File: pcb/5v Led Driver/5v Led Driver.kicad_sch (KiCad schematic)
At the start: 43 parts, among them J1 USB_C_Receptacle_USB2.0_16P, J2 Conn_01x02_Pin, J3 Conn_01x02_Pin, J4 Conn_01x03_Pin, J5 Conn_01x02_Pin, SW2 PTS815 SJM 250 SMTR LFS, U1 RP2040, U2 W25Q16JVUXIQ TR, U3 RT6150B-33GQW, Y1 ABM8G-12.000MHZ-B4Y-T

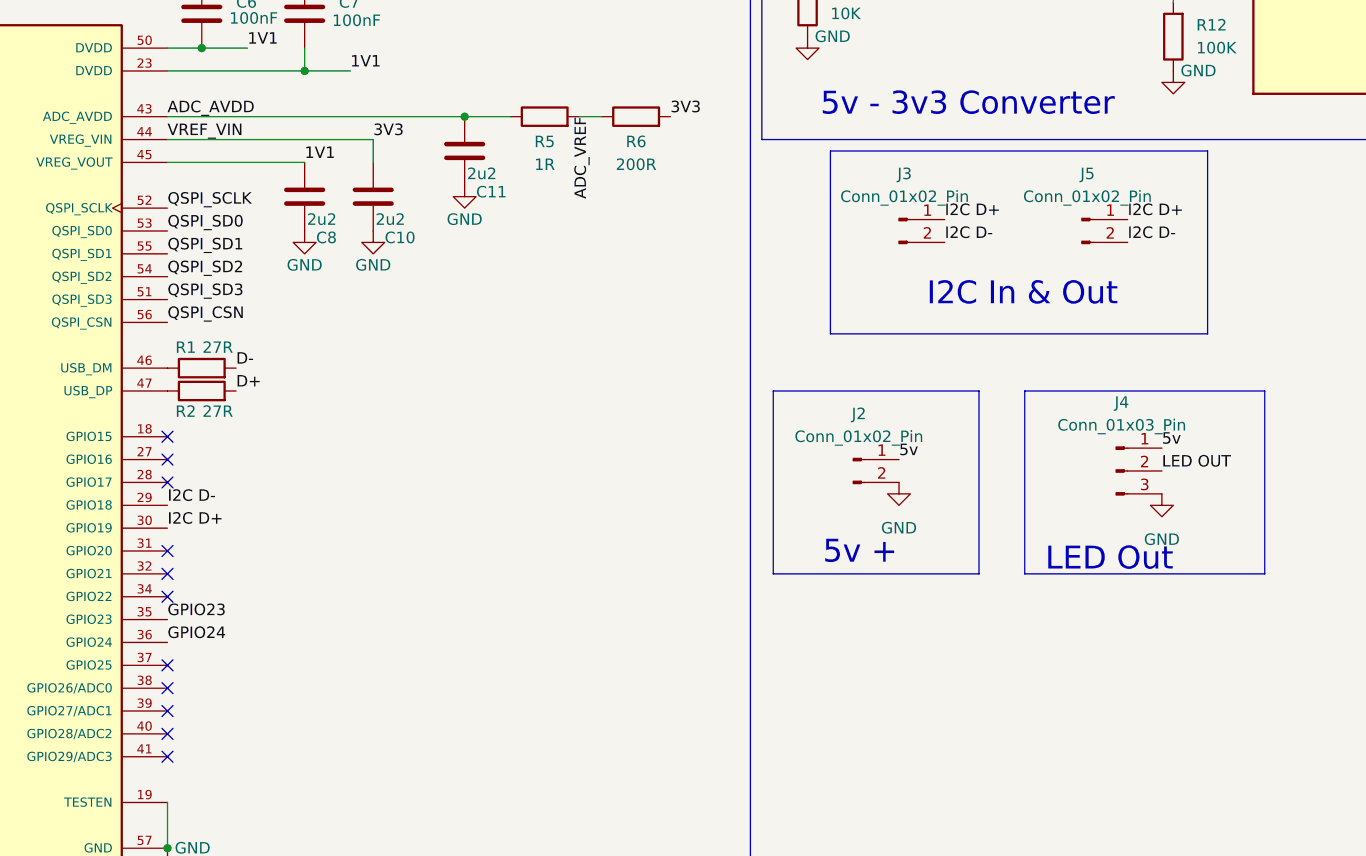
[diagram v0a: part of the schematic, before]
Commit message: cant access pwmRead
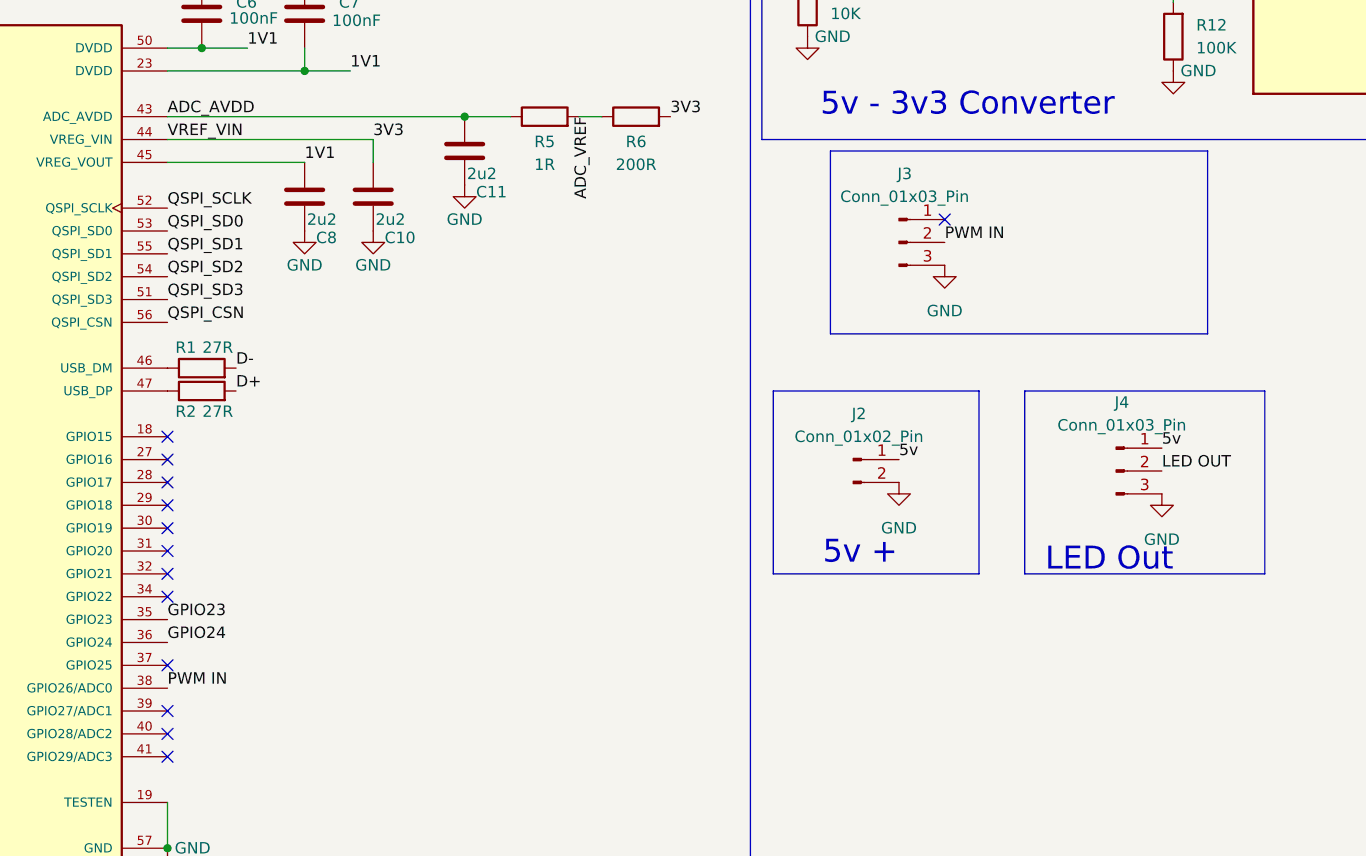
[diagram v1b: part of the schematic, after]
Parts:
- removed J3, J5: Conn_01x02_Pin, Connector_PinHeader_2.54mm:PinHeader_1x02_P2.54mm_Horizontal, symbol Connector:Conn_01x02_Pin
- added J3: Conn_01x03_Pin, Connector_PinHeader_2.54mm:PinHeader_1x03_P2.54mm_Horizontal, symbol Connector:Conn_01x03_Pin
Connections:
- net GND: now also J3.3 (Pin_3)
- net PWM IN: now reaches U1.38 (GPIO26/ADC0)
- net PWM IN: now also J3.2 (Pin_2)
- net I2C D+: no longer names the net of U1.30 (GPIO19)
- net I2C D-: no longer names the net of U1.29 (GPIO18)
- no-connect marks 32 -> 34
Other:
- note removed: "I2C In & Out"
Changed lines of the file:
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@@
 	)
 	(no_connect
+		(at 109.22 148.59)
+	)
+	(no_connect
 		(at 63.5 118.11)
 	)
@@
 	)
 	(no_connect
-		(at 109.22 166.37)
-	)
-	(no_connect
 		(at 63.5 156.21)
 	)
@@
 	)
 	(no_connect
+		(at 195.58 114.3)
+	)
+	(no_connect
 		(at 63.5 120.65)
 	)
@@
 	)
 	(no_connect
+		(at 109.22 146.05)
+	)
+	(no_connect
 		(at 63.5 143.51)
 	)
@@
 		)
 	)
-	(text "I2C In & Out"
-		(exclude_from_sim no)
-		(at 204.216 122.682 0)
-		(effects
-			(font
-				(size 2.54 2.54)
-			)
-		)
-	)
 	(text "MicroController"
 		(exclude_from_sim no)
@@
 		)
 	)
+	(label "PWM IN"
+		(at 109.22 166.37 0)
+		(fields_autoplaced yes)
+		(effects
+			(font
+				(size 1.27 1.27)
+			)
+			(justify left bottom)
+		)
+	)
 	(label "RUN"
 		(at 63.5 180.34 180)
@@
 		)
 	)
-	(label "I2C D-"
-		(at 109.22 146.05 0)
-		(fields_autoplaced yes)
-		(effects
-			(font
-				(size 1.27 1.27)
-			)
-			(justify left bottom)
-		)
-	)
-	(label "I2C D+"
-		(at 195.58 114.3 0)
-		(fields_autoplaced yes)
-		(effects
-			(font
-				(size 1.27 1.27)
-			)
-			(justify left bottom)
-		)
-	)
 	(label "LED OUT"
 		(at 63.5 140.97 180)
@@
 		)
 	)
-	(label "I2C D+"
-		(at 109.22 148.59 0)
-		(fields_autoplaced yes)
-		(effects
-			(font
-				(size 1.27 1.27)
-			)
-			(justify left bottom)
-		)
-	)
 	(label "3V3"
 		(at 22.86 95.25 0)
@@
 		)
 	)
+	(label "PWM IN"
+		(at 195.58 116.84 0)
+		(fields_autoplaced yes)
+		(effects
+			(font
+				(size 1.27 1.27)
+			)
+			(justify left bottom)
+		)
+	)
 	(label "3V3_EN"
 		(at 198.12 86.36 0)
@@
 		)
 	)
-	(label "I2C D+"
-		(at 215.9 114.3 0)
-		(fields_autoplaced yes)
-		(effects
-			(font
-				(size 1.27 1.27)
-			)
-			(justify left bottom)
-		)
-	)
 	(label "QSPI_SCLK"
 		(at 185.42 54.61 0)
@@
 		)
 	)
-	(label "I2C D-"
-		(at 195.58 116.84 0)
-		(fields_autoplaced yes)
-		(effects
-			(font
-				(size 1.27 1.27)
-			)
-			(justify left bottom)
-		)
-	)
-	(label "I2C D-"
-		(at 215.9 116.84 0)
-		(fields_autoplaced yes)
-		(effects
-			(font
-				(size 1.27 1.27)
-			)
-			(justify left bottom)
-		)
-	)
 	(label "QSPI_SD3"
 		(at 185.42 52.07 0)
@@
 	)
 	(symbol
-		(lib_id "Connector:Conn_01x02_Pin")
-		(at 210.82 114.3 0)
-		(unit 1)
-		(exclude_from_sim no)
-		(in_bom yes)
-		(on_board yes)
-		(dnp no)
-		(fields_autoplaced yes)
-		(property "Reference" "J5"
-			(at 211.455 109.22 0)
-			(effects
-				(font
-					(size 1.27 1.27)
-				)
-			)
-		)
-		(property "Value" "Conn_01x02_Pin"
-			(at 211.455 111.76 0)
-			(effects
-				(font
-					(size 1.27 1.27)
-				)
-			)
-		)
-		(property "Footprint" "Connector_PinHeader_2.54mm:PinHeader_1x02_P2.54mm_Horizontal"
-			(at 210.82 114.3 0)
-			(effects
-				(font
-					(size 1.27 1.27)
-				)
-				(hide yes)
-			)
-		)
-		(property "Datasheet" "~"
-			(at 210.82 114.3 0)
-			(effects
-				(font
-					(size 1.27 1.27)
-				)
-				(hide yes)
-			)
-		)
-		(property "Description" "Generic connector, single row, 01x02, script generated"
-			(at 210.82 114.3 0)
-			(effects
-				(font
-					(size 1.27 1.27)
-				)
-				(hide yes)
-			)
-		)
-		(pin "2"
-		)
-		(pin "1"
-		)
-		(instances
-			(project "5v Led Driver"
-				(path "/2f979bd2-f254-4a27-81cb-7765d8524067"
-					(reference "J5")
-					(unit 1)
-				)
-			)
-		)
-	)
-	(symbol
 		(lib_id "power:GND")
 		(at 29.21 115.57 0)
@@
 	(symbol
 		(lib_id "power:GND")
+		(at 195.58 119.38 0)
+		(unit 1)
+		(exclude_from_sim no)
+		(in_bom yes)
+		(on_board yes)
+		(dnp no)
+		(property "Reference" "#PWR030"
+			(at 195.58 125.73 0)
+			(effects
+				(font
+					(size 1.27 1.27)
+				)
+				(hide yes)
+			)
+		)
+		(property "Value" "GND"
+			(at 195.58 124.46 0)
+			(effects
+				(font
+					(size 1.27 1.27)
+				)
+			)
+		)
+		(property "Footprint" ""
+			(at 195.58 119.38 0)
+			(effects
+				(font
+					(size 1.27 1.27)
+				)
+				(hide yes)
+			)
+		)
+		(property "Datasheet" ""
+			(at 195.58 119.38 0)
+			(effects
+				(font
+					(size 1.27 1.27)
+				)
+				(hide yes)
+			)
+		)
+		(property "Description" "Power symbol creates a global label with name \"GND\" , ground"
+			(at 195.58 119.38 0)
+			(effects
+				(font
+					(size 1.27 1.27)
+				)
+				(hide yes)
+			)
+		)
+		(pin "1"
+		)
+		(instances
+			(project "5v Led Driver"
+				(path "/2f979bd2-f254-4a27-81cb-7765d8524067"
+					(reference "#PWR030")
+					(unit 1)
+				)
+			)
+		)
+	)
+	(symbol
+		(lib_id "power:GND")
 		(at 124.46 115.57 0)
 		(unit 1)
@@
 	)
 	(symbol
+		(lib_id "Connector:Conn_01x03_Pin")
+		(at 190.5 116.84 0)
+		(unit 1)
+		(exclude_from_sim no)
+		(in_bom yes)
+		(on_board yes)
+		(dnp no)
+		(fields_autoplaced yes)
+		(property "Reference" "J3"
+			(at 191.135 109.22 0)
+			(effects
+				(font
+					(size 1.27 1.27)
+				)
+			)
+		)
+		(property "Value" "Conn_01x03_Pin"
+			(at 191.135 111.76 0)
+			(effects
+				(font
+					(size 1.27 1.27)
+				)
+			)
+		)
+		(property "Footprint" "Connector_PinHeader_2.54mm:PinHeader_1x03_P2.54mm_Horizontal"
+			(at 190.5 116.84 0)
+			(effects
+				(font
+					(size 1.27 1.27)
+				)
+				(hide yes)
+			)
+		)
+		(property "Datasheet" "~"
+			(at 190.5 116.84 0)
+			(effects
+				(font
+					(size 1.27 1.27)
+				)
+				(hide yes)
+			)
+		)
+		(property "Description" "Generic connector, single row, 01x03, script generated"
+			(at 190.5 116.84 0)
+			(effects
+				(font
+					(size 1.27 1.27)
+				)
+				(hide yes)
+			)
+		)
+		(pin "3"
+		)
+		(pin "2"
+		)
+		(pin "1"
+		)
+		(instances
+			(project ""
+				(path "/2f979bd2-f254-4a27-81cb-7765d8524067"
+					(reference "J3")
+					(unit 1)
+				)
+			)
+		)
+	)
+	(symbol
 		(lib_id "Connector:Conn_01x02_Pin")
 		(at 185.42 140.97 0)
@@
 					(unit 1)
 				)
-			)
-		)
-	)
-	(symbol
-		(lib_id "Connector:Conn_01x02_Pin")
-		(at 190.5 114.3 0)
-		(unit 1)
-		(exclude_from_sim no)
-		(in_bom yes)
-		(on_board yes)
-		(dnp no)
-		(fields_autoplaced yes)
-		(property "Reference" "J3"
-			(at 191.135 109.22 0)
-			(effects
-				(font
-					(size 1.27 1.27)
-				)
-			)
-		)
-		(property "Value" "Conn_01x02_Pin"
-			(at 191.135 111.76 0)
-			(effects
-				(font
-					(size 1.27 1.27)
-				)
-			)
-		)
-		(property "Footprint" "Connector_PinHeader_2.54mm:PinHeader_1x02_P2.54mm_Horizontal"
-			(at 190.5 114.3 0)
-			(effects
-				(font
-					(size 1.27 1.27)
-				)
-				(hide yes)
-			)
-		)
-		(property "Datasheet" "~"
-			(at 190.5 114.3 0)
-			(effects
-				(font
-					(size 1.27 1.27)
-				)
-				(hide yes)
-			)
-		)
-		(property "Description" "Generic connector, single row, 01x02, script generated"
-			(at 190.5 114.3 0)
-			(effects
-				(font
-					(size 1.27 1.27)
-				)
-				(hide yes)
-			)
-		)
-		(pin "2"
-		)
-		(pin "1"
-		)
-		(instances
-			(project "5v Led Driver"
-				(path "/2f979bd2-f254-4a27-81cb-7765d8524067"
-					(reference "J3")
-					(unit 1)
-				)
